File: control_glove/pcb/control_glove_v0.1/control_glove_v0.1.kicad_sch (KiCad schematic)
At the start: 14 parts, among them P1 Power_Pins, SW1 SW_Push, SW2 SW_Push, U1 UART-RF433

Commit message: update: Complete list and connect all components
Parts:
- removed IMU1, IMU2: GY-87, symbol hieu_lib:GY-87
- added BZ1: Buzzer, Buzzer_Beeper:Buzzer_12x9.5RM7.6, symbol Device:Buzzer
- added IMU1, IMU2: GY-521, Connector_PinHeader_2.54mm:PinHeader_1x08_P2.54mm_Vertical, symbol hieu_lib:GY-521
- added MARG1, MARG2: HMC5883L, Connector_PinHeader_2.54mm:PinHeader_1x05_P2.54mm_Vertical, symbol hieu_lib:HMC5883L
- added Q1: Q_NPN_ECB, Package_TO_SOT_THT:TO-92_Inline, symbol Device:Q_NPN_ECB
- added R5: 330, Resistor_THT:R_Axial_DIN0207_L6.3mm_D2.5mm_P7.62mm_Horizontal, symbol Device:R
- added R6: 300, Resistor_THT:R_Axial_DIN0207_L6.3mm_D2.5mm_P7.62mm_Horizontal, symbol Device:R
- D1, D2: footprint (none) -> LED_THT:LED_D3.0mm
- MCU1: footprint (none) -> Connector_PinHeader_2.54mm:PinHeader_2x20_P2.54mm_Vertical
- P1, SW1, SW2: footprint (none) -> TerminalBlock:TerminalBlock_Altech_AK300-2_P5.00mm
- R1, R2, R3, R4: footprint (none) -> Resistor_THT:R_Axial_DIN0207_L6.3mm_D2.5mm_P7.62mm_Horizontal
- RV1: footprint (none) -> TerminalBlock:TerminalBlock_Altech_AK300-3_P5.00mm
- U1: footprint (none) -> Connector_PinHeader_2.54mm:PinHeader_1x05_P2.54mm_Vertical
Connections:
- net 3.3V: now also MCU1.18 (3.3V), R5.1; no longer MCU1. (VB), RV1.1
- net 5V: now also MCU1.20 (5V), U1.1 (VCC); no longer MCU1. (VB), U1. (VCC)
- net GND: now also MCU1.22 (GND), P1.2 (GND), U1.2 (GND), BZ1.2 (+), Q1.1 (E); no longer MCU1. (VB), P1. (GND), U1. (VCC)
- net LED_GREEN: now also MCU1.26 (B1); no longer MCU1. (VB)
- net LED_RED: now also MCU1.27 (B0); no longer MCU1. (VB)
- net RV1: now also MCU1.35 (A0); no longer MCU1. (VB)
- net RX: now also MCU1.7 (A10), U1.4 (TXD); no longer MCU1. (VB), U1. (VCC)
- net SCL1: now also MCU1.14 (B6), IMU1.3 (SCL), MARG1.3 (SCL); no longer MCU1. (VB)
- net SCL2: now also MCU1.24 (B10), IMU2.3 (SCL), MARG2.3 (SCL); no longer MCU1. (VB)
- net SDA1: now also MCU1.15 (B7), IMU1.4 (SDA), MARG1.4 (SDA); no longer MCU1. (VB)
- net SDA2: now also MCU1.11 (B3), IMU2.4 (SDA), MARG2.4 (SDA); no longer MCU1. (VB)
- net SET_UART: now also MCU1.28 (A7), U1.5 (SET); no longer MCU1. (VB), U1. (VCC)
- net SW1: now also MCU1.34 (A1); no longer MCU1. (VB)
- net SW2: now also MCU1.33 (A2); no longer MCU1. (VB)
- net TX: now also MCU1.6 (A9), U1.3 (RXD); no longer MCU1. (VB), U1. (VCC)
- new net: R5.2, RV1.1
- new net: Q1.3 (B), R6.2
- new net: MCU1.21 (5V), P1.1 (5V)
- new net BUZZER: BZ1.1 (-), MCU1.29 (A6)
- new net SENSOR-3.3V: IMU1.1 (VCC), IMU2.1 (VCC), MARG1.1 (VCC), MARG2.1 (VCC), MCU1.23 (3V3)
- new net SENSOR-GND: IMU1.2 (GND), IMU2.2 (GND), MARG1.2 (GND), MARG2.2 (GND), Q1.2 (C)
- new net SENSOR-PWR-EN: MCU1.25 (B2), R6.1
- no-connect marks 24 -> 23
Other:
- note added: "CONTROL_GLOVE_v0.1"
- moved on the sheet: D1, D2, R1, R2, R3, R4, RV1, SW1, SW2

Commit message: update: PCB setup and arange component positions
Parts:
- removed RV1: 10K, TerminalBlock:TerminalBlock_Altech_AK300-3_P5.00mm, symbol Device:R_Potentiometer
- removed SW1, SW2: SW_Push, TerminalBlock:TerminalBlock_Altech_AK300-2_P5.00mm, symbol Switch:SW_Push
- added H1, H10, H11, H12, H2, H3, H4, H5, H6, H7, H8, H9: MountingHole, MountingHole:MountingHole_3.2mm_M3, symbol Mechanical:MountingHole
- added J1, J2, J7, J8: Conn_01x04_Female, Connector_PinSocket_2.00mm:PinSocket_1x04_P2.00mm_Vertical, symbol Connector:Conn_01x04_Female
- added J3, J4, J5, J6: Conn_01x03_Female, Connector_PinSocket_2.00mm:PinSocket_1x03_P2.00mm_Vertical, symbol Connector:Conn_01x03_Female
- added JP1: Jumper_3_Bridged12, Connector_PinHeader_2.54mm:PinHeader_1x03_P2.54mm_Vertical, symbol Jumper:Jumper_3_Bridged12
- added R7: 1K, Resistor_THT:R_Axial_DIN0207_L6.3mm_D2.5mm_P7.62mm_Horizontal, symbol Device:R
- added R8: 300, Resistor_THT:R_Axial_DIN0207_L6.3mm_D2.5mm_P7.62mm_Horizontal, symbol Device:R
- added SW3: SW_Push, Button_Switch_THT:SW_PUSH_6mm_H13mm, symbol Switch:SW_Push
- MCU1: footprint Connector_PinHeader_2.54mm:PinHeader_2x20_P2.54mm_Vertical -> hieu:stm32f4_board
- P1: footprint TerminalBlock:TerminalBlock_Altech_AK300-2_P5.00mm -> TerminalBlock_TE-Connectivity:TerminalBlock_TE_282834-2_1x02_P2.54mm_Horizontal
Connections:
- net 3.3V: now also R7.1
- net BUZZER: now also R8.1; no longer BZ1.1 (-)
- net GND: now also J3.3 (Pin_3), J4.1 (Pin_1), JP1.2 (C), SW3.1
- net RV1: now also J4.2 (Pin_2)
- net SCL1: now also J1.2 (Pin_2); no longer IMU1.3 (SCL), MARG1.3 (SCL)
- net SCL2: now also J2.2 (Pin_2); no longer IMU2.3 (SCL), MARG2.3 (SCL)
- net SDA1: now also J1.3 (Pin_3); no longer IMU1.4 (SDA), MARG1.4 (SDA)
- net SDA2: now also J2.3 (Pin_3); no longer IMU2.4 (SDA), MARG2.4 (SDA)
- net SENSOR-3.3V: now also J1.1 (Pin_1), J2.1 (Pin_1); no longer IMU1.1 (VCC), IMU2.1 (VCC), MARG1.1 (VCC), MARG2.1 (VCC)
- net SENSOR-GND: now also J1.4 (Pin_4), J2.4 (Pin_4), JP1.1 (A); no longer IMU1.2 (GND), IMU2.2 (GND), MARG1.2 (GND), MARG2.2 (GND), Q1.2 (C)
- net SW1: now also J3.2 (Pin_2)
- net SW2: now also J3.1 (Pin_1)
- net at R5.2: now also J4.3 (Pin_3)
- net SW3: now reaches MCU1.32 (A3)
- net SW3: now also R7.2, SW3.2
- new net: J5.1 (Pin_1), J6.1 (Pin_1)
- new net: J5.2 (Pin_2), J6.2 (Pin_2)
- new net: J5.3 (Pin_3), J6.3 (Pin_3)
- new net: IMU1.1 (VCC), J8.4 (Pin_4), MARG1.1 (VCC)
- new net: IMU1.2 (GND), J8.3 (Pin_3), MARG1.2 (GND)
- new net: IMU1.3 (SCL), J8.2 (Pin_2), MARG1.3 (SCL)
- new net: IMU1.4 (SDA), J8.1 (Pin_1), MARG1.4 (SDA)
- new net: IMU2.1 (VCC), J7.4 (Pin_4), MARG2.1 (VCC)
- new net: IMU2.2 (GND), J7.3 (Pin_3), MARG2.2 (GND)
- new net: IMU2.3 (SCL), J7.2 (Pin_2), MARG2.3 (SCL)
- new net: IMU2.4 (SDA), J7.1 (Pin_1), MARG2.4 (SDA)
- new net: JP1.3 (B), Q1.2 (C)
- new net: BZ1.1 (-), R8.2
- no-connect marks 23 -> 22
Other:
- note added: "HAND MODULE"
- note added: "MAIN MODULE"
- note added: "SHOULDER MODULE"
- note removed: "CONTROL_GLOVE_v0.1"
- moved on the sheet: BZ1, D1, D2, IMU2, MARG2, MCU1, P1, Q1, R1, R2, R3, R4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

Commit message: update: Complete connect all components on PCB
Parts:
- added R10, R11, R12, R13, R14, R9: 0, Resistor_THT:R_Axial_DIN0207_L6.3mm_D2.5mm_P7.62mm_Horizontal, symbol Device:R
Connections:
- net 3.3V: now also J2.1 (Pin_1); no longer R5.1
- net 5V: now also R9.1; no longer U1.1 (VCC)
- net SENSOR-GND: now also R10.1, R12.1; no longer J2.4 (Pin_4), JP1.1 (A)
- net SET_UART: now also R13.1; no longer U1.5 (SET)
- net SENSOR-3.3V renamed 3.3V-SHOULDER
- net 3.3V-SHOULDER: now also R5.1; no longer J2.1 (Pin_1)
- new net: J2.4 (Pin_4), R11.2
- new net: R11.1, R12.2
- new net: JP1.1 (A), R10.2
- new net: R9.2, U1.1 (VCC)
- new net: R14.2, U1.5 (SET)
- new net: R13.2, R14.1
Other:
- moved on the sheet: J2, U1

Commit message: update: Complete fix pcb
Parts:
- SW3: footprint Button_Switch_THT:SW_PUSH_6mm_H13mm -> Resistor_THT:R_Axial_DIN0207_L6.3mm_D2.5mm_P7.62mm_Horizontal
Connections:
- net GND: now also JP1.1 (A); no longer JP1.2 (C)
- net at R10.2: now also JP1.2 (C); no longer JP1.1 (A)
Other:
- moved on the sheet: R10

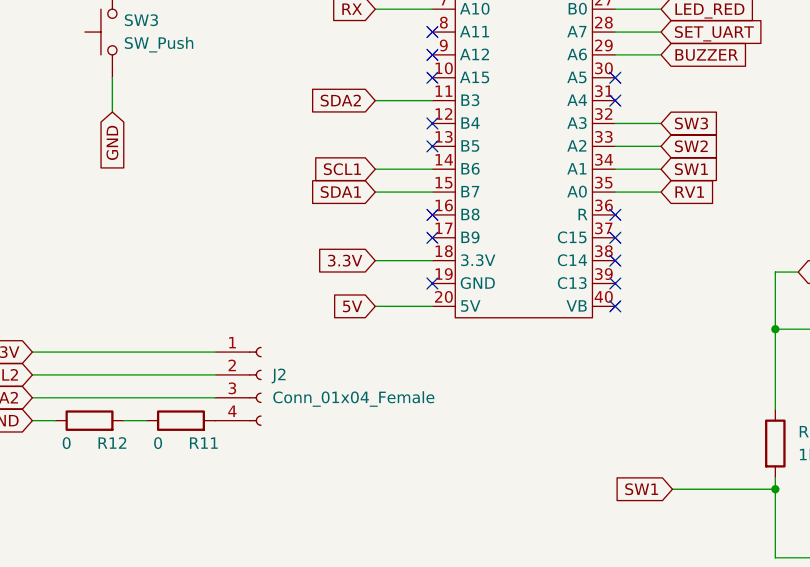
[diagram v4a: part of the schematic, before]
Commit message: update: Test Control Glove v0.1 PCB success
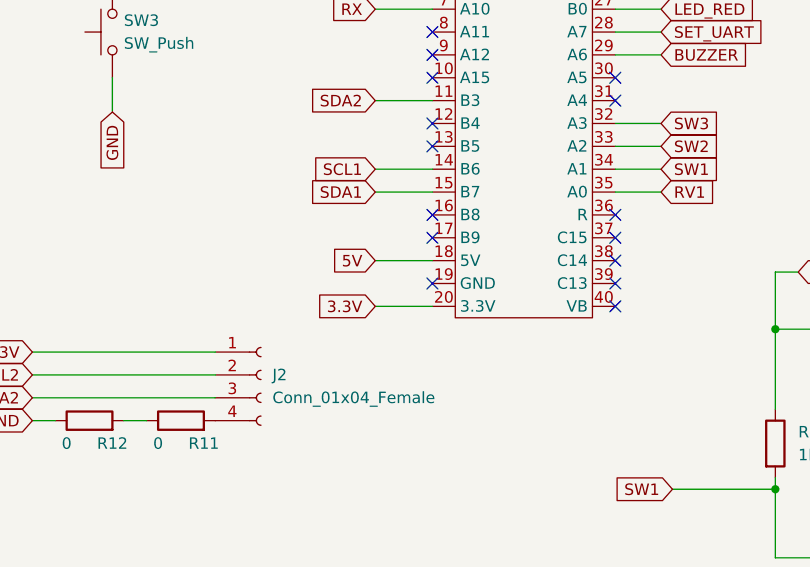
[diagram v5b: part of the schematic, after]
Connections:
- net 3.3V: now also MCU1.20 (3.3V); no longer MCU1.18 (3.3V)
- net 5V: now also MCU1.18 (5V); no longer MCU1.20 (5V)
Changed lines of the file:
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@@
     )
   )
-  (global_label "3.3V" (shape input) (at 137.16 93.98 180) (fields_autoplaced)
+  (global_label "5V" (shape input) (at 137.16 93.98 180) (fields_autoplaced)
     (effects (font (size 1.27 1.27)) (justify right))
-    (property "Intersheet References" "${INTERSHEET_REFS}" (id 0) (at 130.6345 94.0594 0)
+    (property "Intersheet References" "${INTERSHEET_REFS}" (id 0) (at 132.4488 93.9006 0)
       (effects (font (size 1.27 1.27)) (justify right) hide)
     )
@@
     )
   )
-  (global_label "5V" (shape input) (at 137.16 99.06 180) (fields_autoplaced)
+  (global_label "3.3V" (shape input) (at 137.16 99.06 180) (fields_autoplaced)
     (effects (font (size 1.27 1.27)) (justify right))
-    (property "Intersheet References" "${INTERSHEET_REFS}" (id 0) (at 132.4488 99.1394 0)
+    (property "Intersheet References" "${INTERSHEET_REFS}" (id 0) (at 130.6345 98.9806 0)
       (effects (font (size 1.27 1.27)) (justify right) hide)
     )

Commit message: update: Add switch and trigger button and remove unused components
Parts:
- removed BZ1: Buzzer, Buzzer_Beeper:Buzzer_12x9.5RM7.6, symbol Device:Buzzer
- removed JP1: Jumper_3_Bridged12, Connector_PinHeader_2.54mm:PinHeader_1x03_P2.54mm_Vertical, symbol Jumper:Jumper_3_Bridged12
- removed Q1: Q_NPN_ECB, Package_TO_SOT_THT:TO-92_Inline, symbol Device:Q_NPN_ECB
- removed R10: 0, Resistor_THT:R_Axial_DIN0207_L6.3mm_D2.5mm_P7.62mm_Horizontal, symbol Device:R
- removed R6, R8: 300, Resistor_THT:R_Axial_DIN0207_L6.3mm_D2.5mm_P7.62mm_Horizontal, symbol Device:R
- added JP1: Jumper_2_Bridged, Connector_PinHeader_2.54mm:PinHeader_1x02_P2.54mm_Vertical, symbol Jumper:Jumper_2_Bridged
- added SW5: SW_DIP_x01, hieu:resistor, symbol Switch:SW_DIP_x01
- added SW_6: SW_Push, hieu:resistor, symbol Switch:SW_Push
- P1: footprint TerminalBlock_TE-Connectivity:TerminalBlock_TE_282834-2_1x02_P2.54mm_Horizontal -> Connector_PinSocket_2.00mm:PinSocket_1x03_P2.00mm_Vertical
- R1, R11, R12, R13, R14, R2, R3, R4, R5, R7, R9, SW3: footprint Resistor_THT:R_Axial_DIN0207_L6.3mm_D2.5mm_P7.62mm_Horizontal -> hieu:resistor
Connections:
- net GND: now also JP1.2 (B), SW_6.2
- net at R11.1, R12.2: now also JP1.1 (A)
- net at P1.1 (5V): now also SW5.1; no longer MCU1.21 (5V)
- net BUZZER: no longer names the net of MCU1.29 (A6)
- net SENSOR-PWR-EN: no longer names the net of MCU1.25 (B2)
- new net: P1.3 (K), SW_6.1
- new net: MCU1.21 (5V), SW5.2
- no-connect marks 22 -> 24
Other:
- moved on the sheet: J3, MCU1, R1, R12, R2
